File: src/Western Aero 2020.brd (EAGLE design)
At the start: 133.7 x 108.9 mm, 95 parts, among them IC1 LT1963AET, IC2 LT1963AET, J1 PITOT, J10 ANA_IO, J11 PWR, J2 BUZZER, J3 RX2/TX2, J4 RX3/TX3, J5 SPI, J6 DIG_IO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

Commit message: Finished re-route
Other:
- board size 133.7 x 108.9 mm -> 115.7 x 105.4 mm
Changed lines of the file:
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@@
 <board>
 <plain>
-<wire x1="-1.5" y1="0.5" x2="132.24" y2="0" width="0" layer="20"/>
-<wire x1="132.24" y1="0" x2="132.24" y2="108.87" width="0" layer="20"/>
-<wire x1="132.24" y1="108.87" x2="-1.5" y2="108.87" width="0" layer="20"/>
-<wire x1="-1.5" y1="108.87" x2="-1.5" y2="0.5" width="0" layer="20"/>
+<wire x1="-1.5" y1="0.5" x2="114.24" y2="0.375" width="0" layer="20"/>
+<wire x1="114.24" y1="0.375" x2="114.24" y2="105.695" width="0" layer="20"/>
+<wire x1="114.24" y1="105.695" x2="-1.5" y2="105.795" width="0" layer="20"/>
+<wire x1="-1.5" y1="105.795" x2="-1.5" y2="0.5" width="0" layer="20"/>
 <text x="80.5" y="2.5" size="2.54" layer="21" align="center">Jeff St. Jean</text>
 <text x="43" y="94.5" size="2.54" layer="21" align="center">Western Engineering

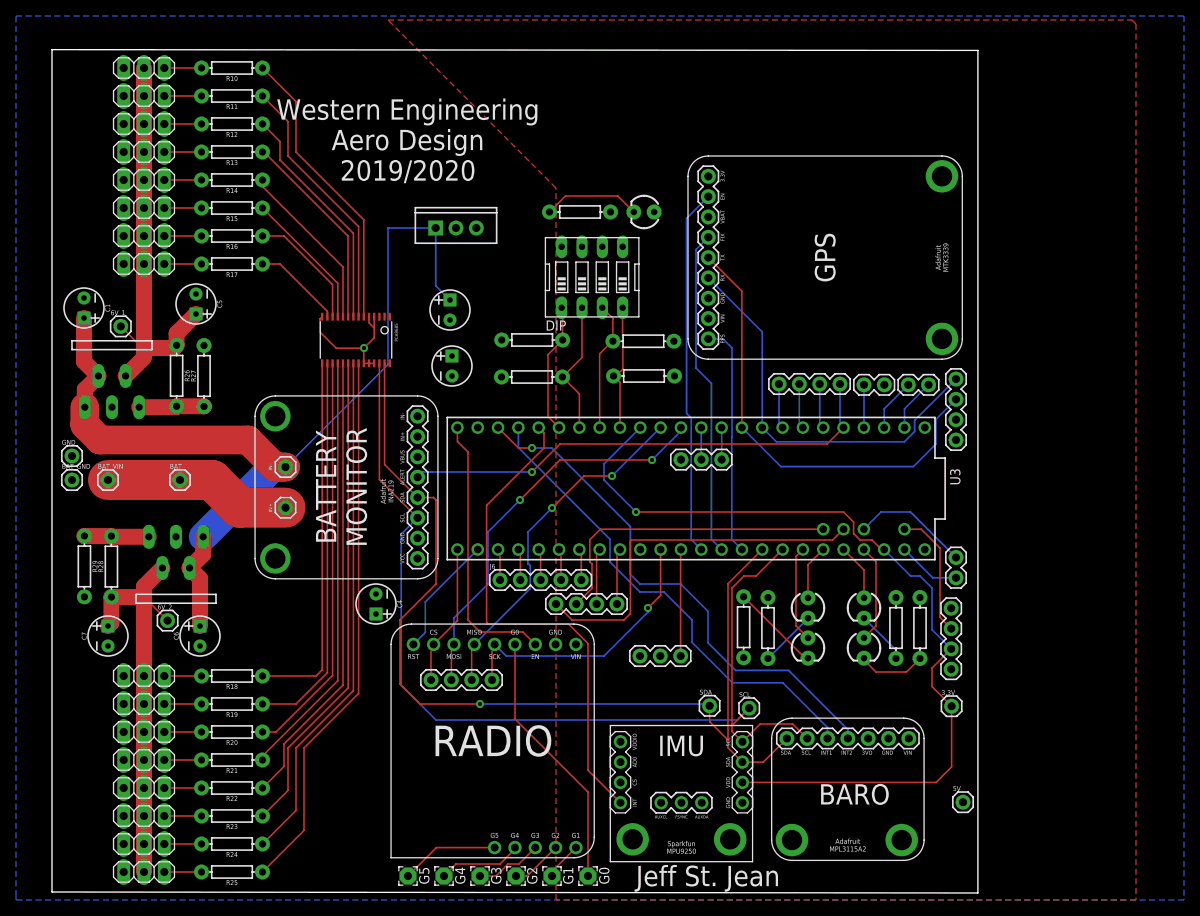
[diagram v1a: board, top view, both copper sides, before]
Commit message: Trace adjustments
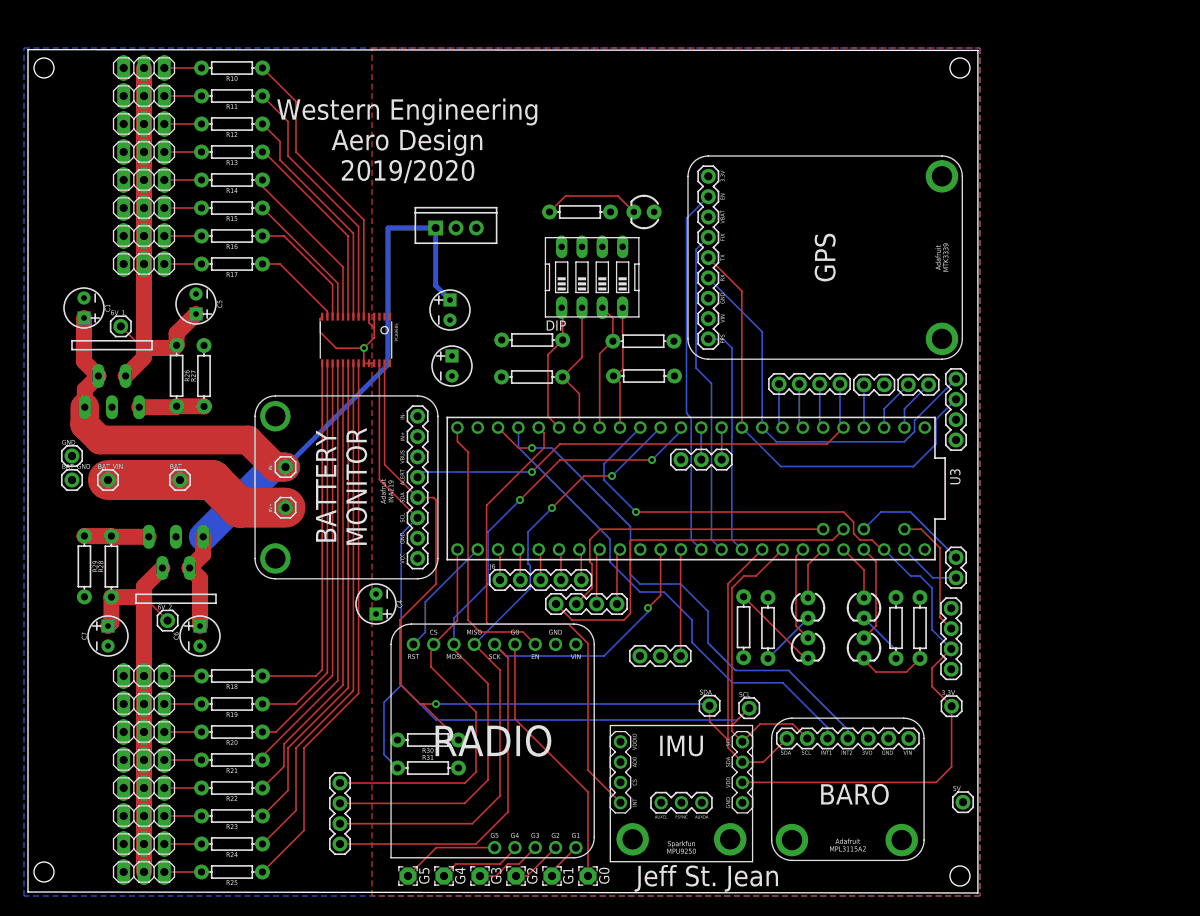
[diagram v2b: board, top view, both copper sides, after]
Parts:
- added R30: 4.7k, SparkFun-Resistors:AXIAL-0.3
- added R31: 4.7K, SparkFun-Resistors:AXIAL-0.3
- moved J5 28.0 mm to (34.5, 6.50), turned to 90 degrees
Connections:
- net 5V: now also R30.P$2, R31.P$2
- net SCL: now also R31.P$1
- net SDA: now also R30.P$1
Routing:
- net SCK: track 35.1 -> 74.8 mm
- net MISO: track 43.7 -> 80.8 mm
- net MOSI: track 50.2 -> 84.3 mm
- net CS: track 17.7 -> 49.1 mm
- net SCL: track 129.9 -> 141.8 mm
- net SDA: track 126.7 -> 133.1 mm
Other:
- board size 115.7 x 105.4 mm -> 118.7 x 105.4 mm
